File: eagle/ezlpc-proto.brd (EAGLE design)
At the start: 30.5 x 25.4 mm, 62 parts, among them J1 MICRO USB, Q1 12Mhz, T1 MMBT3906, U1 PRTR5V0U2X, U2 MIC5225-3.3v, U3 LPC11U35FHN33/501

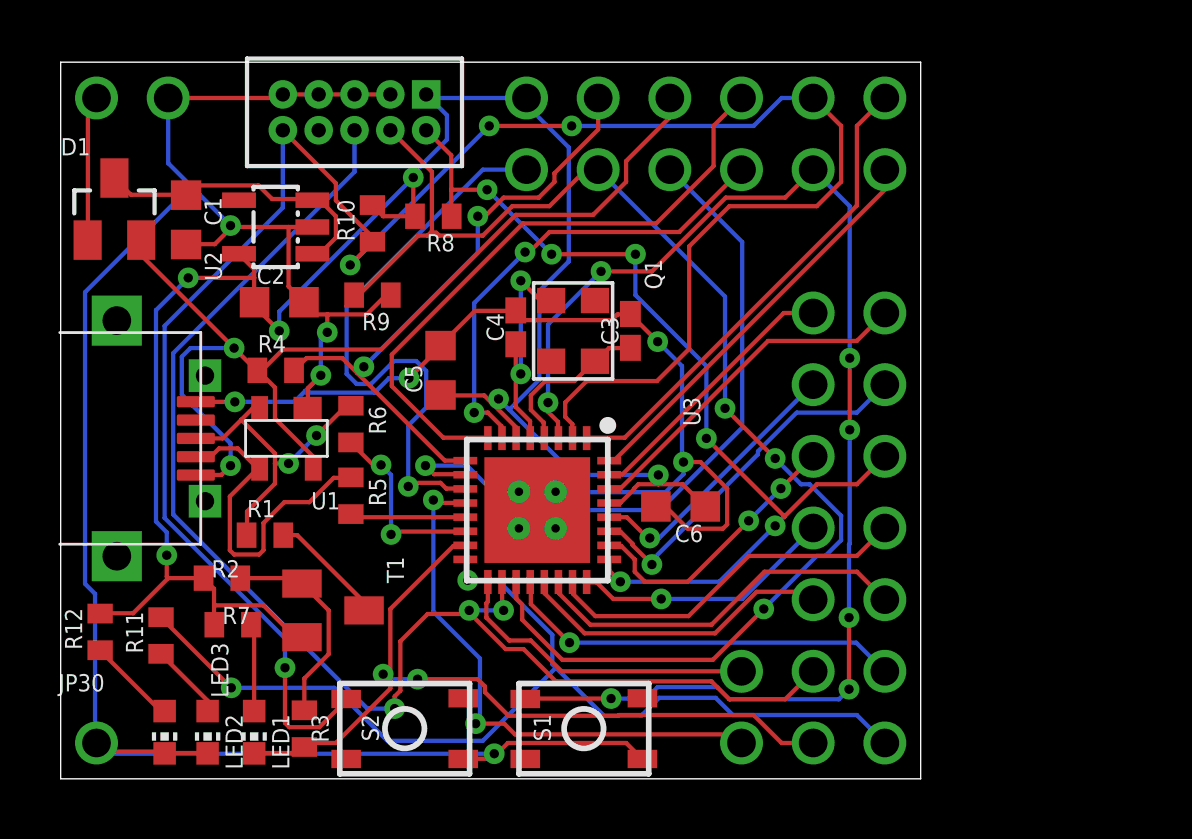
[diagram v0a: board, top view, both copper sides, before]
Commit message: Imprived the placement. Now can auto route 100%.
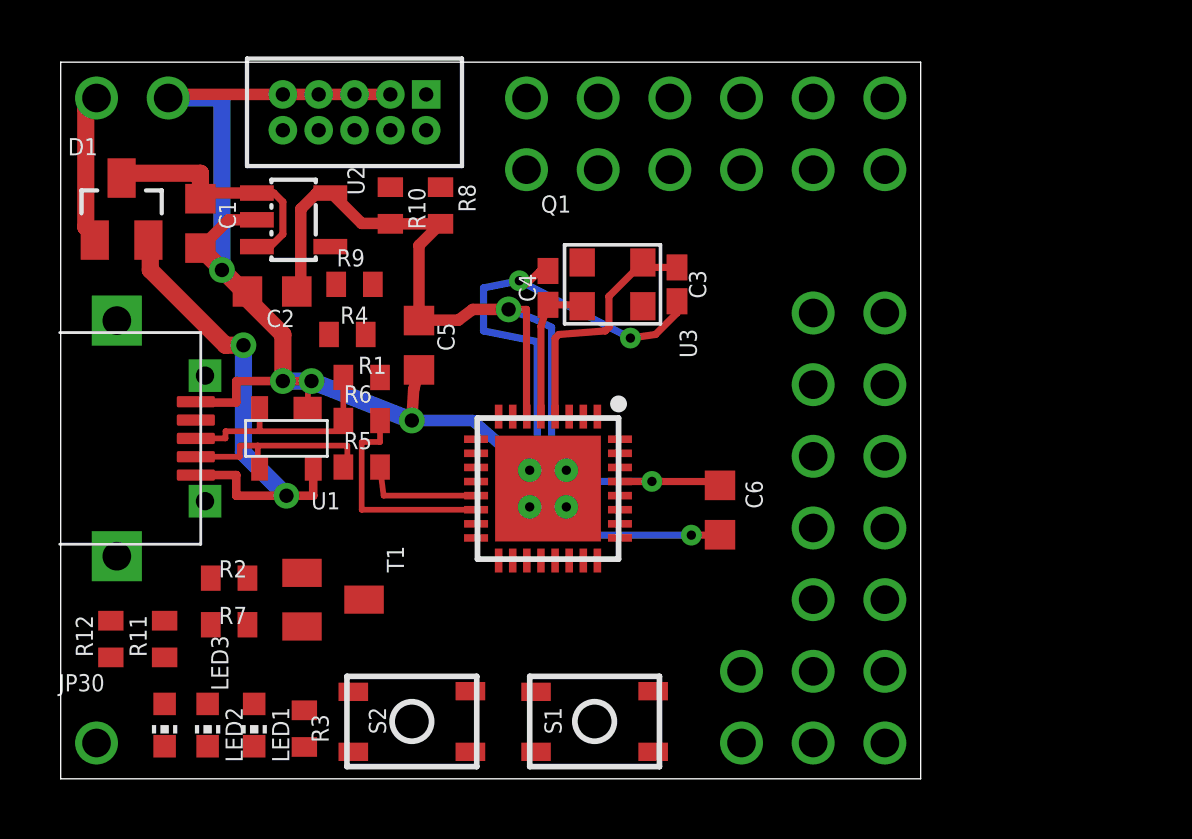
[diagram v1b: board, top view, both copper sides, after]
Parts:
- moved R1 6.56 mm to (10.7, 14.2)
- moved R4 2.84 mm to (10.2, 15.7)
- moved C3 2.33 mm to (21.8, 17.5), turned to 270 degrees
- moved Q1 2.16 mm to (19.6, 17.5), turned to 0 degrees
- moved C4 1.81 mm to (17.3, 17.4)
- moved C6 1.40 mm to (23.4, 9.53), turned to 270 degrees
- moved C5 1.17 mm to (12.7, 15.4), turned to 270 degrees
- moved R5 1.09 mm to (10.7, 11.0), turned to 0 degrees
- moved R10 0.90 mm to (11.7, 20.3), turned to 270 degrees
- moved U3 0.85 mm to (17.3, 10.3)
- moved R9 0.74 mm to (10.4, 17.5), turned to 0 degrees
- moved U2 0.68 mm to (8.26, 19.8), turned to 270 degrees
- moved C1 0.52 mm to (4.95, 19.7)
- moved C2 0.46 mm to (7.49, 17.3), turned to 180 degrees
- moved R8 0.46 mm to (13.5, 20.3), turned to 270 degrees
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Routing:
- net PIO0_0-RESET: track 72.3 -> 0.00 mm, vias 4 -> 0
- net PIO0_9: track 48.6 -> 0.00 mm, vias 3 -> 0
- net PIO0_1-ISP_EN: track 46.8 -> 0.00 mm, vias 7 -> 0
- net PIO0_10-SWDCLK: track 46.8 -> 0.00 mm, vias 3 -> 0
- net GND: track 113.9 -> 70.9 mm, vias 8 -> 7
- net +3V3: track 72.1 -> 34.5 mm, vias 6 -> 2
- net PIO0_7-LED: track 36.0 -> 0.00 mm, vias 2 -> 0
- net PIO0_15-SWDIO: track 34.6 -> 0.00 mm, vias 6 -> 0
- net PIO0_6-CONNECT: track 28.8 -> 0.00 mm, vias 2 -> 0
- net PIO0_4: track 24.8 -> 0.00 mm, vias 1 -> 0
- net PIO0_2: track 22.3 -> 0.00 mm
- net PIO0_3-VBUS: track 21.9 -> 0.00 mm, vias 2 -> 0
- net PIO0_5: track 20.8 -> 0.00 mm, vias 1 -> 0
- net USB-5V: track 38.0 -> 17.3 mm
- net PIO0_21: track 19.6 -> 0.00 mm, vias 2 -> 0
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
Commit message: Minor layout cleanups.
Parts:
- moved R9 13.2 mm to (13.0, 4.57), turned to 180 degrees
- moved JP9 5.08 mm to (24.1, 1.27)
- moved JP23 2.54 mm to (26.7, 1.27)
- moved JP8 2.54 mm to (29.2, 1.27)
- moved C3 2.33 mm to (20.2, 15.9), turned to 180 degrees
- moved R5 1.15 mm to (10.5, 9.91)
- moved C4 0.92 mm to (18.2, 17.7)
- moved Q1 0.92 mm to (20.4, 17.8)
- moved R8 0.77 mm to (12.7, 20.4)
- moved C5 0.74 mm to (13.1, 16.0)
- moved R10 0.52 mm to (11.2, 20.4)
- moved R4 0.18 mm to (10.0, 15.6)
- moved R6 0.18 mm to (10.5, 12.6)
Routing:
- net GND: track 70.9 -> 68.1 mm
- net +3V3: track 34.5 -> 31.7 mm
- net USB_DM: track 4.30 -> 3.55 mm
- net N$3: track 5.23 -> 5.92 mm
- net N$9: track 7.56 -> 8.23 mm
- net USB_DP: track 7.87 -> 8.38 mm

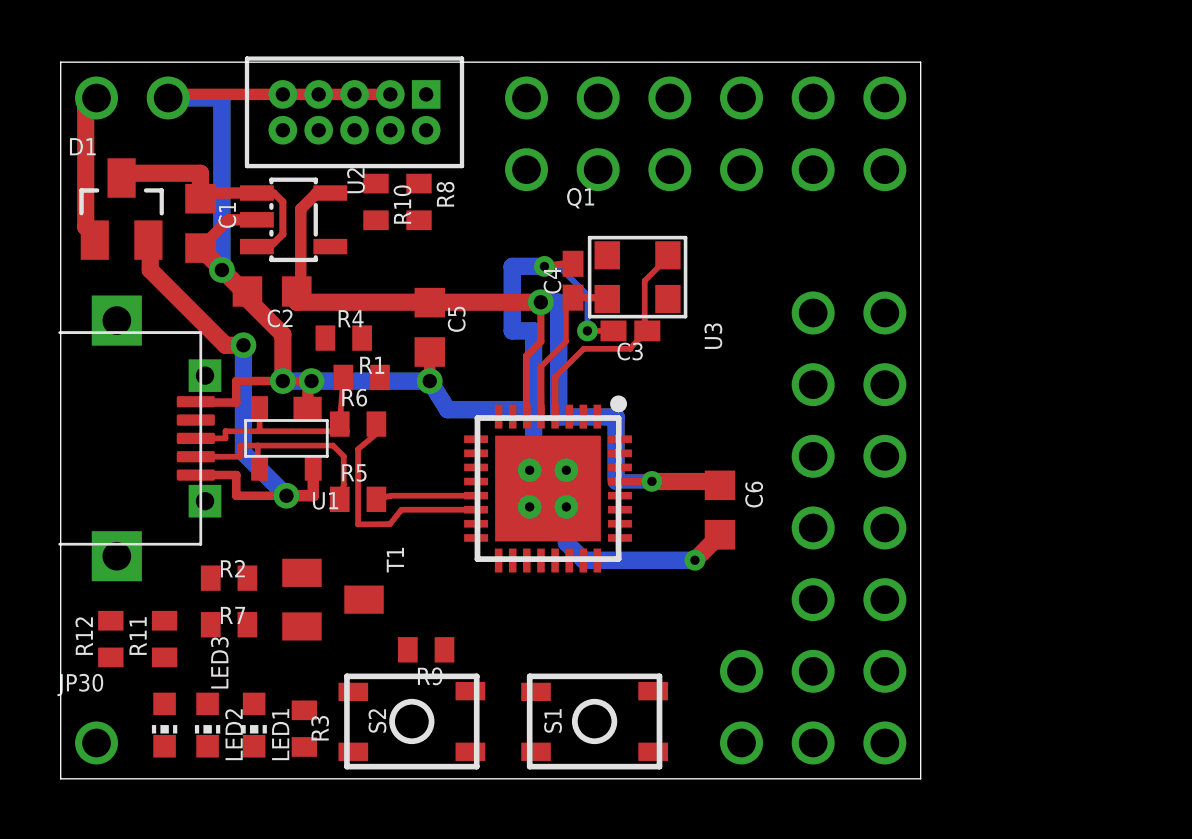
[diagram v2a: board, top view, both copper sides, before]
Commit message: Extracted self library from the schema.
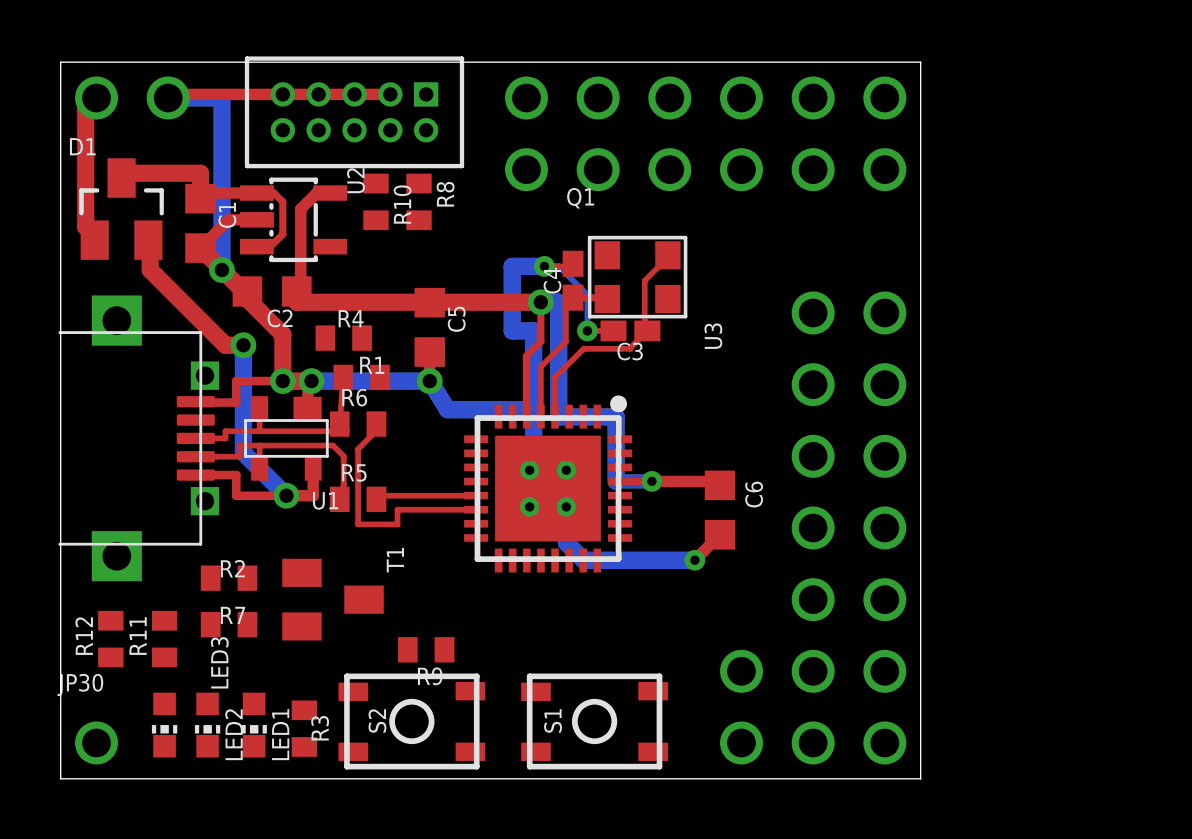
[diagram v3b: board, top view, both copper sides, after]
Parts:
- C1, C2: device rcl:C0603K -> ezlpc-proto:CAPACITOR-0603K
- T1: device transistor-pnp:SOT23-BEC -> ezlpc-proto:SOT23-BEC
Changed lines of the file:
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@@
 <param name="rvMicroViaOuter" value="0.25"/>
 <param name="rvMicroViaInner" value="0.25"/>
-<param name="rlMinPadTop" value="10mil"/>
+<param name="rlMinPadTop" value="7mil"/>
 <param name="rlMaxPadTop" value="20mil"/>
 <param name="rlMinPadInner" value="10mil"/>
@@
 <attribute name="VALUE" x="4.826" y="21.717" size="1.27" layer="27" rot="R270"/>
 </element>
-<element name="C2" library="rcl" package="C0603K" value="2u2" x="7.493" y="17.272" smashed="yes" rot="R180">
+<element name="C2" library="ezlpc-proto" package="CAPACITOR-0603K" value="2u2" x="7.493" y="17.272" smashed="yes" rot="R180">
 <attribute name="NAME" x="8.293" y="16.622" size="0.6096" layer="25" rot="R180"/>
 <attribute name="VALUE" x="8.293" y="18.922" size="1.016" layer="27" rot="R180"/>
 </element>
-<element name="C1" library="rcl" package="C0603K" value="2u2" x="4.953" y="19.685" smashed="yes" rot="R270">
+<element name="C1" library="ezlpc-proto" package="CAPACITOR-0603K" value="2u2" x="4.953" y="19.685" smashed="yes" rot="R270">
 <attribute name="NAME" x="5.603" y="20.485" size="0.6096" layer="25" rot="R270"/>
 <attribute name="VALUE" x="3.303" y="20.485" size="1.016" layer="27" rot="R270"/>
@@
 <attribute name="VALUE" x="0" y="-1.905" size="1.27" layer="27"/>
 </element>
-<element name="T1" library="transistor-pnp" package="SOT23-BEC" value="MMBT3906" x="9.652" y="6.35" smashed="yes" rot="R270">
+<element name="T1" library="ezlpc-proto" package="SOT23-BEC" value="MMBT3906" x="9.652" y="6.35" smashed="yes" rot="R270">
 <attribute name="NAME" x="11.557" y="8.255" size="0.6096" layer="25" rot="R270"/>
 <attribute name="VALUE" x="6.477" y="8.255" size="1.27" layer="27" rot="R270"/>
@@
 <wire x1="6.223" y1="13.335" x2="6.223" y2="14.097" width="0.3048" layer="1"/>
 <wire x1="6.223" y1="14.097" x2="7.874" y2="14.097" width="0.3048" layer="1"/>
-<wire x1="7.874" y1="14.097" x2="8.763" y2="14.097" width="0.3048" layer="1"/>
+<wire x1="7.874" y1="14.097" x2="8.763" y2="14.097" width="0.6096" layer="1"/>
 <wire x1="8.763" y1="14.097" x2="8.763" y2="13.14" width="0.4064" layer="1"/>
 <wire x1="8.763" y1="13.14" x2="8.751" y2="13.14" width="0.2032" layer="1"/>
@@
 <via x="22.479" y="7.747" extent="1-16" drill="0.3302"/>
 <wire x1="17.922" y1="10.414" x2="17.922" y2="10.937" width="0.254" layer="16"/>
-<wire x1="18.161" y1="18.253" x2="17.872" y2="18.253" width="0.254" layer="1"/>
-<wire x1="17.872" y1="18.253" x2="17.145" y2="18.161" width="0.254" layer="1"/>
+<wire x1="18.161" y1="18.253" x2="18.161" y2="18.161" width="0.2032" layer="1"/>
+<wire x1="18.161" y1="18.161" x2="17.145" y2="18.161" width="0.2032" layer="1"/>
 <via x="17.145" y="18.161" extent="1-16" drill="0.3302"/>
 <via x="18.669" y="15.875" extent="1-16" drill="0.3302"/>
-<wire x1="22.479" y1="7.747" x2="23.354" y2="8.636" width="0.6096" layer="1"/>
+<wire x1="22.479" y1="7.747" x2="23.354" y2="8.636" width="0.4064" layer="1"/>
 <wire x1="23.354" y1="8.636" x2="23.368" y2="8.65" width="0.254" layer="1"/>
 <wire x1="13.081" y1="14.097" x2="13.081" y2="15.127" width="0.4064" layer="1"/>
@@
 <contactref element="U3" pad="4"/>
 <contactref element="Q1" pad="3"/>
-<wire x1="17.522" y1="12.837" x2="17.522" y2="14.224" width="0.254" layer="1"/>
+<wire x1="17.522" y1="12.837" x2="17.522" y2="14.224" width="0.2032" layer="1"/>
 <wire x1="21.697" y1="18.38" x2="21.522" y2="18.555" width="0.254" layer="1"/>
 <wire x1="17.522" y1="14.224" x2="18.538" y2="15.24" width="0.2032" layer="1"/>
@@
 <contactref element="U3" pad="5"/>
 <contactref element="Q1" pad="1"/>
-<wire x1="17.022" y1="12.837" x2="17.018" y2="14.605" width="0.254" layer="1"/>
+<wire x1="17.022" y1="12.837" x2="17.018" y2="14.605" width="0.2032" layer="1"/>
 <wire x1="18.161" y1="17.053" x2="19.324" y2="17.053" width="0.254" layer="1"/>
 <wire x1="19.324" y1="17.053" x2="19.372" y2="17.005" width="0.254" layer="1"/>
@@
 <wire x1="13.081" y1="16.877" x2="13.208" y2="16.891" width="0.4064" layer="1"/>
 <wire x1="20.955" y1="10.541" x2="19.685" y2="10.541" width="0.508" layer="16"/>
-<wire x1="23.368" y1="10.537" x2="20.959" y2="10.537" width="0.6096" layer="1"/>
+<wire x1="23.368" y1="10.537" x2="20.959" y2="10.537" width="0.4064" layer="1"/>
 <wire x1="20.959" y1="10.537" x2="20.955" y2="10.541" width="0.6096" layer="1"/>
 <wire x1="19.822" y1="10.537" x2="20.951" y2="10.537" width="0.254" layer="1"/>
@@
 <contactref element="U3" pad="13"/>
 <wire x1="14.722" y1="10.037" x2="14.722" y2="10.033" width="0.2032" layer="1"/>
-<wire x1="14.722" y1="10.033" x2="11.699" y2="10.033" width="0.2032" layer="1"/>
-<wire x1="11.699" y1="10.033" x2="11.191" y2="9.906" width="0.2032" layer="1"/>
+<wire x1="14.722" y1="10.033" x2="11.191" y2="10.033" width="0.2032" layer="1"/>
+<wire x1="11.191" y1="10.033" x2="11.191" y2="9.906" width="0.2032" layer="1"/>
 </signal>
 <signal name="USB_DP" class="2">
 <contactref element="R6" pad="2"/>
 <contactref element="U3" pad="14"/>
-<wire x1="12.08" y1="9.537" x2="14.722" y2="9.537" width="0.2032" layer="1"/>
+<wire x1="11.938" y1="9.537" x2="14.722" y2="9.537" width="0.2032" layer="1"/>
 <wire x1="11.191" y1="12.573" x2="11.318" y2="12.334" width="0.2032" layer="1"/>
-<wire x1="11.318" y1="12.334" x2="10.541" y2="11.684" width="0.2032" layer="1"/>
 <wire x1="10.541" y1="11.684" x2="10.541" y2="9.017" width="0.2032" layer="1"/>
-<wire x1="10.541" y1="9.017" x2="11.672" y2="9.029" width="0.2032" layer="1"/>
-<wire x1="11.672" y1="9.029" x2="12.08" y2="9.537" width="0.2032" layer="1"/>
+<wire x1="11.938" y1="9.017" x2="10.541" y2="9.017" width="0.2032" layer="1"/>
+<wire x1="10.541" y1="11.684" x2="11.191" y2="12.334" width="0.2032" layer="1"/>
+<wire x1="11.191" y1="12.334" x2="11.191" y2="12.573" width="0.2032" layer="1"/>
+<wire x1="11.938" y1="9.017" x2="11.938" y2="9.537" width="0.2032" layer="1"/>
 </signal>
 <signal name="N$9">
@@
 <wire x1="4.79" y1="11.415" x2="6.35" y2="11.415" width="0.2032" layer="1"/>
 <wire x1="6.35" y1="11.415" x2="6.35" y2="11.811" width="0.2032" layer="1"/>
-<wire x1="6.35" y1="11.811" x2="6.985" y2="11.811" width="0.2032" layer="1"/>
-<wire x1="7.051" y1="10.99" x2="6.985" y2="10.99" width="0.2032" layer="1"/>
-<wire x1="6.985" y1="10.99" x2="6.985" y2="11.811" width="0.2032" layer="1"/>
-<wire x1="6.985" y1="11.811" x2="9.652" y2="11.811" width="0.2032" layer="1"/>
+<wire x1="6.35" y1="11.811" x2="7.051" y2="11.811" width="0.2032" layer="1"/>
+<wire x1="7.112" y1="11.811" x2="9.652" y2="11.811" width="0.2032" layer="1"/>
 <wire x1="9.652" y1="11.811" x2="10.033" y2="11.43" width="0.2032" layer="1"/>
 <wire x1="10.033" y1="11.43" x2="10.033" y2="10.429" width="0.2032" layer="1"/>
 <wire x1="10.033" y1="10.429" x2="9.891" y2="9.906" width="0.2032" layer="1"/>
+<wire x1="7.051" y1="10.99" x2="7.051" y2="11.811" width="0.2032" layer="1"/>
+<wire x1="7.051" y1="11.811" x2="7.112" y2="11.811" width="0.2032" layer="1"/>
 </signal>
 <signal name="N$11">

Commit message: Ready for final auto routing.
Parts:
- removed JP32: (no value), ezlpc-proto:1X01
- moved JP1 24.4 mm to (36.2, 16.9)
- moved S2 23.9 mm to (34.9, 10.2)
- moved JP23 22.9 mm to (3.81, 1.27)
- moved JP9 22.9 mm to (1.27, 1.27)
- moved LED3 22.0 mm to (19.6, 17.1), turned to 270 degrees
- moved JP30 20.5 mm to (3.81, 21.6)
- moved JP8 20.3 mm to (8.89, 1.27)
- moved R8 20.0 mm to (26.3, 5.71), turned to 180 degrees
- moved R12 18.9 mm to (16.8, 16.5), turned to 270 degrees
- moved JP10 18.0 mm to (6.35, 1.27)
- moved JP19 17.0 mm to (36.8, 1.27)
- moved S1 16.4 mm to (34.9, 5.71)
- moved JP11 15.5 mm to (11.4, 1.27)
- moved JP24 15.5 mm to (14.0, 1.27)
- moved JP26 14.8 mm to (34.3, 1.27)
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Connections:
- net GND: no longer JP32.1
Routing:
- net USB_DM: track 3.66 -> 9.22 mm
- net USB_DP: track 8.80 -> 12.5 mm
- net GND: track 68.1 -> 64.8 mm
- net +3V3: track 31.7 -> 34.0 mm
- net N$10: track 9.27 -> 7.27 mm
- net N$9: track 8.16 -> 6.50 mm
- net USB-5V: track 17.3 -> 16.3 mm
- net N$8: track 8.45 -> 7.62 mm
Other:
- board size 30.5 x 25.4 mm -> 38.1 x 22.9 mm
- board text added: "1"
- board text added: "10"
- board text added: "15"
- board text added: "20"
- board text added: "25"
- board text added: "30"
- board text added: "5"
- board text added: "ISP"
- board text added: "LED"
- board text added: "PWR"
- board text added: "RST"
- board text added: "USB"

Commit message: Cleaned up tplace text.
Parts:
- U3: value LPC11U35FHN33/501 -> LPC11U35FHI33/501
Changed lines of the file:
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@@
 <attribute name="VALUE" x="6.224" y="17.818" size="1.016" layer="27" rot="R270"/>
 </element>
-<element name="U3" library="ezlpc-proto" package="HVQFN33-5MM" value="LPC11U35FHN33/501" x="22.733" y="9.144" smashed="yes" rot="R270">
+<element name="U3" library="ezlpc-proto" package="HVQFN33-5MM" value="LPC11U35FHI33/501" x="22.733" y="9.144" smashed="yes" rot="R270">
 <attribute name="NAME" x="24.059" y="12.413" size="0.6096" layer="25" font="vector"/>
 <attribute name="VALUE" x="17.783" y="12.644" size="1.27" layer="27" font="vector" rot="R270"/>
